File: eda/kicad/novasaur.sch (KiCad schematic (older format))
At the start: 29 parts, among them U1 74F86, U10 74F574, U11 74F574, U12 PAL16R4, U2 74F32, U3 74F11, U4 74F139, U5 74F139, U6 74F157, U7 74F175, U8 74F574, U9 74F138, X1 33M

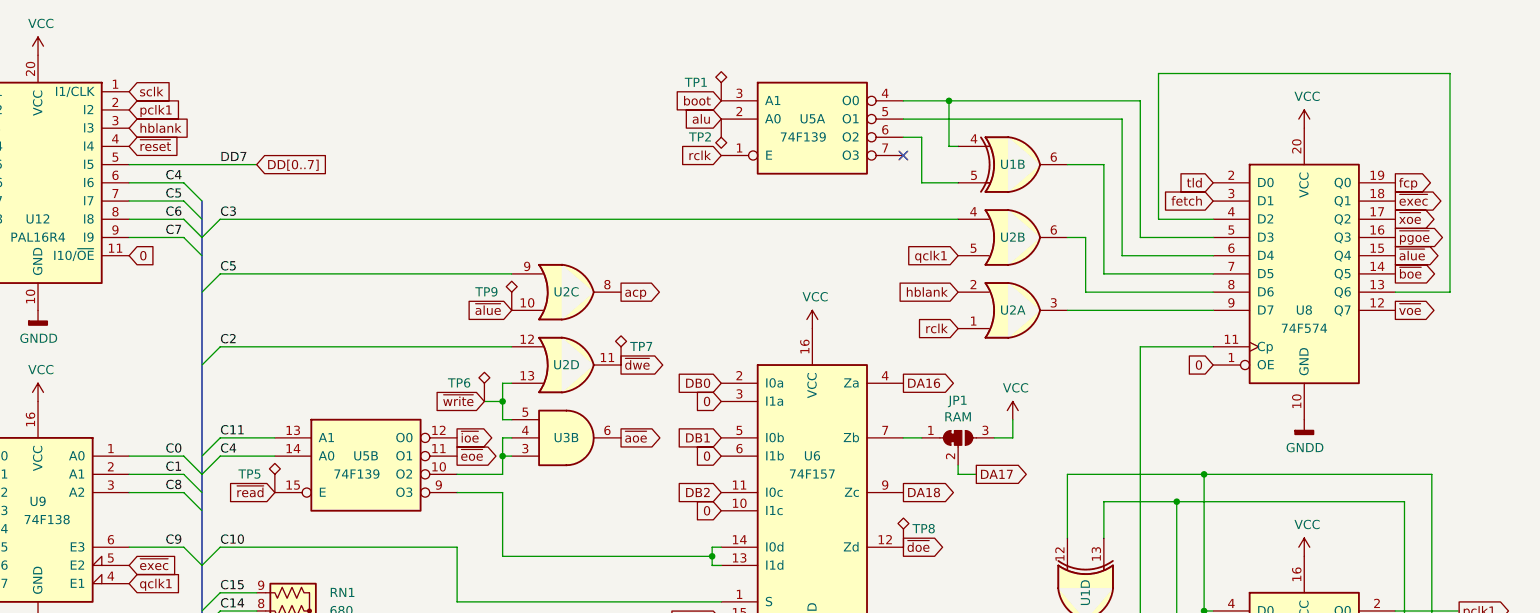
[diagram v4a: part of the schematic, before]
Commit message: roll back to new 6v reg
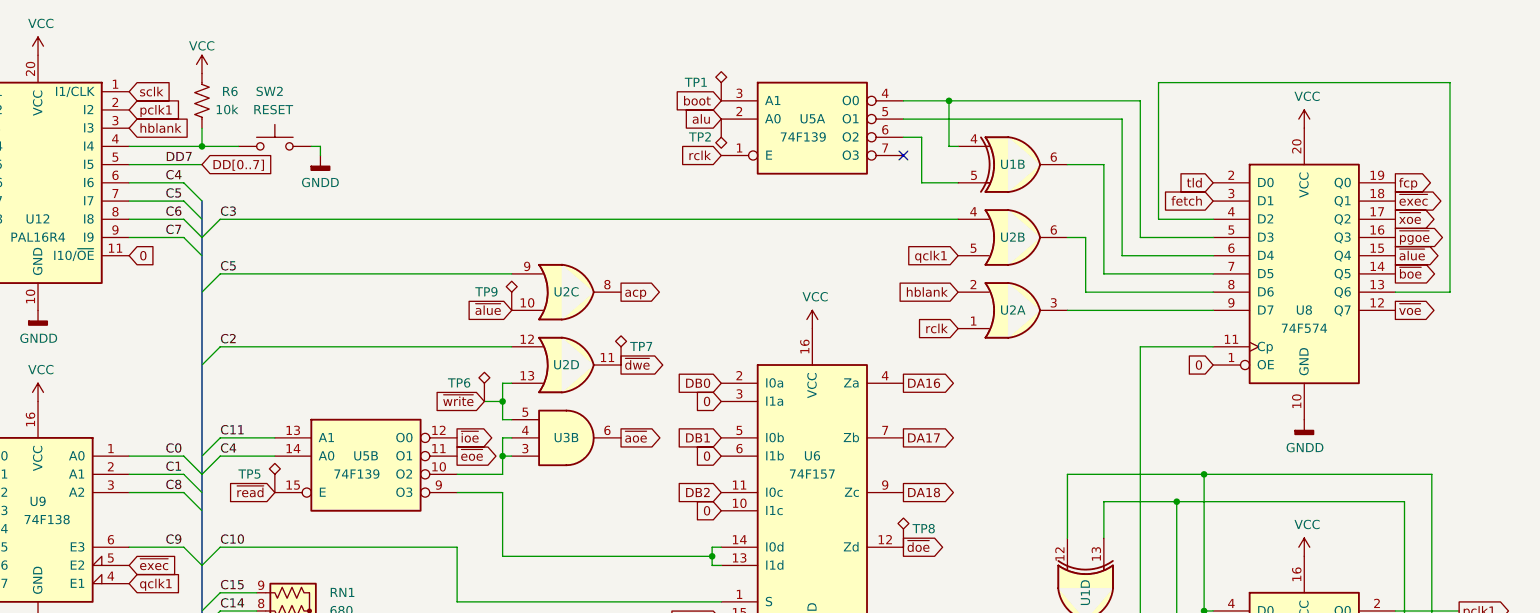
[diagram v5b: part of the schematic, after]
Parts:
- removed JP1: RAM, Jumper:SolderJumper-3_P1.3mm_Bridged12_RoundedPad1.0x1.5mm, symbol Jumper:SolderJumper_3_Bridged12
- added R6: 10k, Resistor_THT:R_Axial_DIN0204_L3.6mm_D1.6mm_P7.62mm_Horizontal, symbol Device:R_US
- added SW2: RESET, Button_Switch_THT:SW_DIP_SPSTx01_Slide_6.7x4.1mm_W7.62mm_P2.54mm_LowProfile, symbol Switch:SW_Push
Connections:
- net DA17: now also U6.7 (Zb)
- net GNDD: now also SW2.1
- net VCC: now also R6.2
- net ~reset: no longer names the net of U12.4 (I4)
- net ~reset: now also R6.1, SW2.2
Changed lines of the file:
@@
 Sheet 1 4
 Title "Novasaur Retrocomputer"
-Date "2021-06-24"
+Date "2021-10-20"
 Rev "1.10"
 Comp ""
@@
 	1    0    0    -1
 $EndComp
-Wire Wire Line
-	9600 1100 8000 1100
 $Comp
 L Connector:TestPoint_Alt TP3
@@
 	7600 4650 7500 4650
 Connection ~ 7600 4650
-Text GLabel 7000 3300 2    50   Output ~ 0
+Text GLabel 6600 3100 2    50   Output ~ 0
 DA17
 Wire Wire Line
 	9600 2300 9300 2300
-Wire Wire Line
-	9600 1100 9600 2300
-Wire Wire Line
-	8000 1100 8000 1900
 Wire Wire Line
 	4400 3000 4400 2900
@@
 	5600 5900 4150 5900
 Connection ~ 4150 5900
-Text GLabel 2350 1500 2    50   Input ~ 0
-~reset
 $Comp
 L Connector:TestPoint_Alt TP28
@@
 F 3 "~" H 4350 5900 50  0001 C CNN
 	1    4150 5900
-	1    0    0    -1
-$EndComp
-Wire Wire Line
-	6600 3100 6700 3100
-$Comp
-L Jumper:SolderJumper_3_Bridged12 JP1
-U 1 1 5EB86903
-P 6900 3100
-F 0 "JP1" H 6900 3305 50  0000 C CNN
-F 1 "RAM" H 6900 3214 50  0000 C CNN
-F 2 "Jumper:SolderJumper-3_P1.3mm_Bridged12_RoundedPad1.0x1.5mm" H 6900 3100 50  0001 C CNN
-F 3 "~" H 6900 3100 50  0001 C CNN
-	1    6900 3100
-	1    0    0    -1
-$EndComp
-Wire Wire Line
-	7000 3300 6900 3300
-Wire Wire Line
-	6900 3300 6900 3250
-Wire Wire Line
-	7100 3100 7200 3100
-Wire Wire Line
-	7200 3100 7200 3000
-$Comp
-L power:VCC #PWR?
-U 1 1 5EAF98E7
-P 7200 3000
-AR Path="/5CDEEC9F/5EAF98E7" Ref="#PWR?"  Part="1"
-AR Path="/5DAA5CD8/5EAF98E7" Ref="#PWR?"  Part="1"
-AR Path="/5EAF98E7" Ref="#PWR0198"  Part="1"
-F 0 "#PWR0198" H 7200 2850 50  0001 C CNN
-F 1 "VCC" H 7217 3173 50  0000 C CNN
-F 2 "" H 7200 3000 50  0001 C CNN
-F 3 "" H 7200 3000 50  0001 C CNN
-	1    7200 3000
 	1    0    0    -1
 $EndComp
@@
 Wire Wire Line
 	9500 4650 9650 4650
-Wire Wire Line
-	2350 1600 3050 1600
-Text Label 2850 1600 0    50   ~ 0
+Text Label 2550 1600 0    50   ~ 0
 DD7
-Text GLabel 3050 1600 2    50   Input ~ 0
+Text GLabel 2750 1600 2    50   Input ~ 0
 DD[0..7]
 $Comp
@@
 Wire Wire Line
 	4150 4000 5600 4000
+$Comp
+L Device:R_US R?
+U 1 1 61FD430E
+P 2750 1250
+AR Path="/62D13D9D/61FD430E" Ref="R?"  Part="1"
+AR Path="/5DAA5CD8/5D9AFF37/61FD430E" Ref="R?"  Part="1"
+AR Path="/5DA1E9C0/61FD430E" Ref="R?"  Part="1"
+AR Path="/61FD430E" Ref="R6"  Part="1"
+F 0 "R6" H 2550 1200 50  0000 L CNN
+F 1 "10k" H 2550 1300 50  0000 L CNN
+F 2 "Resistor_THT:R_Axial_DIN0204_L3.6mm_D1.6mm_P7.62mm_Horizontal" V 2790 1240 50  0001 C CNN
+F 3 "~" H 2750 1250 50  0001 C CNN
+	1    2750 1250
+	-1   0    0    1
+$EndComp
+$Comp
+L Switch:SW_Push SW?
+U 1 1 61FD4314
+P 3150 1500
+AR Path="/5DA1E9C0/61FD4314" Ref="SW?"  Part="1"
+AR Path="/61FD4314" Ref="SW2"  Part="1"
+F 0 "SW2" H 3100 1800 50  0000 L CNN
+F 1 "RESET" H 3050 1700 50  0000 L CNN
+F 2 "Button_Switch_THT:SW_DIP_SPSTx01_Slide_6.7x4.1mm_W7.62mm_P2.54mm_LowProfile" H 3150 1700 50  0001 C CNN
+F 3 "~" H 3150 1700 50  0001 C CNN
+	1    3150 1500
+	-1   0    0    -1
+$EndComp
+Wire Wire Line
+	2750 1500 2750 1400
+Wire Wire Line
+	2350 1500 2750 1500
+$Comp
+L power:GNDD #PWR?
+U 1 1 62E1CD75
+P 3400 1550
+AR Path="/5CDEEC9F/62E1CD75" Ref="#PWR?"  Part="1"
+AR Path="/5DAA5CD8/62E1CD75" Ref="#PWR?"  Part="1"
+AR Path="/62E1CD75" Ref="#PWR0188"  Part="1"
+F 0 "#PWR0188" H 3400 1300 50  0001 C CNN
+F 1 "GNDD" H 3400 1400 50  0000 C CNN
+F 2 "" H 3400 1550 50  0001 C CNN
+F 3 "" H 3400 1550 50  0001 C CNN
+	1    3400 1550
+	1    0    0    -1
+$EndComp
+Wire Wire Line
+	3350 1500 3400 1500
+Wire Wire Line
+	3400 1500 3400 1550
+Connection ~ 2750 1500
+Wire Wire Line
+	2750 1500 2950 1500
+Wire Wire Line
+	8000 1150 9600 1150
+Wire Wire Line
+	8000 1150 8000 1900
+Wire Wire Line
+	9600 1150 9600 2300
+$Comp
+L power:VCC #PWR?
+U 1 1 61743D1E
+P 2750 1100
+AR Path="/5CDEEC9F/61743D1E" Ref="#PWR?"  Part="1"
+AR Path="/5DAA5CD8/61743D1E" Ref="#PWR?"  Part="1"
+AR Path="/61743D1E" Ref="#PWR0111"  Part="1"
+F 0 "#PWR0111" H 2750 950 50  0001 C CNN
+F 1 "VCC" H 2750 1250 50  0000 C CNN
+F 2 "" H 2750 1100 50  0001 C CNN
+F 3 "" H 2750 1100 50  0001 C CNN
+	1    2750 1100
+	1    0    0    -1
+$EndComp
+Wire Wire Line
+	2750 1600 2350 1600
 Wire Bus Line
 	4450 5100 4450 6750

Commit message: tweak schematic; new doc
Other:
- moved on the sheet: TP36, U1D, X1
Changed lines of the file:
@@
 Comment4 ""
 $EndDescr
-Wire Wire Line
-	4650 6000 4650 6700
-Wire Wire Line
-	4250 6000 4250 6550
 Text GLabel 1350 1800 0    50   Output ~ 0
 alu
-Wire Bus Line
-	1150 6850 4350 6850
 Wire Wire Line
 	2450 5700 2650 5700
@@
 	2350 1700 2650 1700
 NoConn ~ 1350 1400
-Entry Bus Bus
-	4350 6850 4450 6750
-Entry Bus Bus
-	1050 6750 1150 6850
 Text GLabel 2350 3900 2    50   Input ~ 0
 qclk1
@@
 Entry Wire Line
 	2650 1700 2750 1800
-Wire Wire Line
-	4250 6000 4150 6000
 $Comp
 L power:GNDD #PWR?
@@
 $EndComp
 Entry Wire Line
-	4450 5100 4350 5000
-Entry Wire Line
-	4450 5200 4350 5100
-Entry Wire Line
-	4450 5300 4350 5200
-Entry Wire Line
-	4450 5800 4350 5700
+	4450 4900 4350 5000
+Entry Wire Line
+	4450 5000 4350 5100
+Entry Wire Line
+	4450 5100 4350 5200
+Entry Wire Line
+	4450 5600 4350 5700
 Text Label 2550 5000 0    50   ~ 0
 C0
@@
 PD[0..7]
 Entry Wire Line
-	4450 5700 4350 5600
-Entry Wire Line
-	4450 5600 4350 5500
-Entry Wire Line
-	4450 5500 4350 5400
-Entry Wire Line
-	4450 5400 4350 5300
+	4450 5500 4350 5600
+Entry Wire Line
+	4450 5400 4350 5500
+Entry Wire Line
+	4450 5300 4350 5400
+Entry Wire Line
+	4450 5200 4350 5300
 Wire Wire Line
 	4150 5000 4350 5000
@@
 	2750 4750 2850 4650
 Wire Wire Line
-	1150 6700 4650 6700
-Wire Wire Line
-	2450 6550 4250 6550
-Wire Wire Line
 	2850 4250 3050 4250
 Wire Wire Line
@@
 Entry Wire Line
 	2850 3200 2750 3300
-Text Notes 3750 7550 0    150  ~ 0
-I/O
-Text Notes 2500 7550 0    150  ~ 0
-GPU
-Text Notes 1300 7550 0    150  ~ 0
-CPU
-$Sheet
-S 1250 7150 600  600
-U 5DA1E9BA
-F0 "sheet5DA1E720" 50
-F1 "novasaur-cpu.sch" 50
-$EndSheet
-$Sheet
-S 2450 7150 600  600
-U 5DA1E9BD
-F0 "sheet5DA1E721" 50
-F1 "novasaur-gpu.sch" 50
-$EndSheet
 Text Label 2850 3700 0    50   ~ 0
 C10
@@
 	1    0    0    -1
 $EndComp
-$Sheet
-S 3650 7150 600  600
-U 5DA1E9C0
-F0 "sheet5DA1E722" 50
-F1 "novasaur-io.sch" 50
-$EndSheet
 $Comp
 L power:VCC #PWR?
@@
 L Connector:TestPoint_Alt TP36
 U 1 1 5E2B88BD
-P 8000 5500
+P 8050 5500
 AR Path="/5E2B88BD" Ref="TP36"  Part="1"
 AR Path="/5DA1E9BA/5E2B88BD" Ref="TP?"  Part="1"
 AR Path="/5DA1E9BD/5E2B88BD" Ref="TP?"  Part="1"
 AR Path="/5DA1E9C0/5E2B88BD" Ref="TP?"  Part="1"
-F 0 "TP36" H 8050 5650 50  0000 L CNN
-F 1 "DCLK" H 7750 5650 50  0001 L CNN
-F 2 "TestPoint:TestPoint_THTPad_1.0x1.0mm_Drill0.5mm" H 8200 5500 50  0001 C CNN
-F 3 "~" H 8200 5500 50  0001 C CNN
-	1    8000 5500
-	1    0    0    -1
-$EndComp
-Wire Wire Line
-	7150 5500 7200 5500
-Wire Wire Line
-	7150 5150 7500 5150
+F 0 "TP36" H 8100 5650 50  0000 L CNN
+F 1 "DCLK" H 7800 5650 50  0001 L CNN
+F 2 "TestPoint:TestPoint_THTPad_1.0x1.0mm_Drill0.5mm" H 8250 5500 50  0001 C CNN
+F 3 "~" H 8250 5500 50  0001 C CNN
+	1    8050 5500
+	1    0    0    -1
+$EndComp
+Wire Wire Line
+	7200 5500 7250 5500
+Wire Wire Line
+	7200 5150 7550 5150
 Wire Wire Line
 	9500 3300 9500 4550
@@
 Wire Wire Line
 	8300 4050 8250 4050
-Text GLabel 7500 4650 0    50   Output ~ 0
+Text GLabel 7600 4650 0    50   Output ~ 0
 nclk
 NoConn ~ 9300 4750
 Wire Wire Line
-	7500 5150 7500 5100
-Connection ~ 7500 5150
-Wire Wire Line
-	7500 5200 7500 5150
+	7550 5150 7550 5100
+Connection ~ 7550 5150
+Wire Wire Line
+	7550 5200 7550 5150
 Wire Wire Line
 	9350 4250 9650 4250
@@
 L Oscillator:CXO_DIP8 X1
 U 1 1 5D9CA9D5
-P 7500 5500
-F 0 "X1" H 7650 5900 50  0000 L CNN
-F 1 "33M" H 7600 5800 50  0000 L CNN
-F 2 "Oscillator:Oscillator_DIP-8" H 7950 5150 50  0001 C CNN
-F 3 "http://cdn-reichelt.de/documents/datenblatt/B400/OSZI.pdf" H 7400 5500 50  0001 C CNN
-	1    7500 5500
+P 7550 5500
+F 0 "X1" H 7700 5900 50  0000 L CNN
+F 1 "33M" H 7650 5800 50  0000 L CNN
+F 2 "Oscillator:Oscillator_DIP-8" H 8000 5150 50  0001 C CNN
+F 3 "http://cdn-reichelt.de/documents/datenblatt/B400/OSZI.pdf" H 7450 5500 50  0001 C CNN
+	1    7550 5500
 	1    0    0    -1
 $EndComp
@@
 L power:GNDD #PWR?
 U 1 1 5D9CBE89
-P 7500 5800
+P 7550 5800
 AR Path="/5CDEEC9F/5D9CBE89" Ref="#PWR?"  Part="1"
 AR Path="/5DAA5CD8/5D9CBE89" Ref="#PWR?"  Part="1"
 AR Path="/5D9CBE89" Ref="#PWR0112"  Part="1"
-F 0 "#PWR0112" H 7500 5550 50  0001 C CNN
-F 1 "GNDD" H 7504 5645 50  0000 C CNN
-F 2 "" H 7500 5800 50  0001 C CNN
-F 3 "" H 7500 5800 50  0001 C CNN
-	1    7500 5800
+F 0 "#PWR0112" H 7550 5550 50  0001 C CNN
+F 1 "GNDD" H 7554 5645 50  0000 C CNN
+F 2 "" H 7550 5800 50  0001 C CNN
+F 3 "" H 7550 5800 50  0001 C CNN
+	1    7550 5800
 	1    0    0    -1
 $EndComp
@@
 L power:VCC #PWR0191
 U 1 1 5D9DED2A
-P 7500 5100
+P 7550 5100
 AR Path="/5D9DED2A" Ref="#PWR0191"  Part="1"
 AR Path="/5DAA5CD8/5D9DED2A" Ref="#PWR?"  Part="1"
-F 0 "#PWR0191" H 7500 4950 50  0001 C CNN
-F 1 "VCC" H 7517 5273 50  0000 C CNN
-F 2 "" H 7500 5100 50  0001 C CNN
-F 3 "" H 7500 5100 50  0001 C CNN
-	1    7500 5100
-	1    0    0    -1
-$EndComp
-Text GLabel 8000 5500 2    50   Output ~ 0
+F 0 "#PWR0191" H 7550 4950 50  0001 C CNN
+F 1 "VCC" H 7567 5273 50  0000 C CNN
+F 2 "" H 7550 5100 50  0001 C CNN
+F 3 "" H 7550 5100 50  0001 C CNN
+	1    7550 5100
+	1    0    0    -1
+$EndComp
+Text GLabel 8050 5500 2    50   Output ~ 0
 dclk
 $Comp
@@
 DB2
 Wire Wire Line
-	7600 4650 7600 4250
+	7700 4650 7700 4250
 $Comp
 L Connector:TestPoint_Alt TP10
@@
 $EndComp
 Wire Wire Line
-	7600 4650 7500 4650
-Connection ~ 7600 4650
+	7700 4650 7600 4650
+Connection ~ 7700 4650
 Text GLabel 6600 3100 2    50   Output ~ 0
 DA17
@@
 	8250 4050 8250 3300
 Wire Wire Line
-	8250 3300 9500 3300
-Wire Wire Line
 	8100 4450 8100 3450
 Connection ~ 8100 3450
 Wire Wire Line
 	8100 4450 8300 4450
-Wire Wire Line
-	8100 3450 9350 3450
 Connection ~ 8250 3300
 Wire Wire Line
-	7900 4850 8300 4850
-Wire Wire Line
-	7500 3650 7500 3300
-Wire Wire Line
-	7500 3300 8250 3300
-Wire Wire Line
-	7700 3650 7700 3450
-Wire Wire Line
-	7700 3450 8100 3450
-Wire Wire Line
-	7900 2600 8300 2600
+	7600 3650 7600 3300
+Wire Wire Line
+	7600 3300 8250 3300
+Wire Wire Line
+	7800 3650 7800 3450
+Wire Wire Line
+	7800 3450 8100 3450
 Wire Wire Line
 	4400 3750 5550 3750
 Wire Wire Line
 	2850 1900 6900 1900
-Wire Wire Line
-	4650 6000 5600 6000
-Wire Wire Line
-	7800 5500 7900 5500
-Connection ~ 7900 5500
-Wire Wire Line
-	7900 5500 8000 5500
 Wire Wire Line
 	4450 3200 4400 3200
@@
 	4400 2900 4400 2800
 Wire Wire Line
-	7150 5150 7150 5500
-Wire Wire Line
-	7900 4850 7900 5500
-Wire Wire Line
-	7600 4650 8300 4650
-Wire Wire Line
-	7900 4850 7900 2600
-Connection ~ 7900 4850
+	7200 5150 7200 5500
+Wire Wire Line
+	7700 4650 8300 4650
 Wire Wire Line
 	4400 3750 4400 3400
@@
 	1    0    0    -1
 $EndComp
-Wire Wire Line
-	1150 6700 1150 5900
-Wire Wire Line
-	1150 5900 1350 5900
 Connection ~ 1350 5900
 Wire Wire Line
@@
 L 74xx:74LS86 U1
 U 4 1 5F86670E
-P 7600 3950
+P 7700 3950
 AR Path="/5F86670E" Ref="U1"  Part="4"
 AR Path="/5DA1E9BD/5F86670E" Ref="U?"  Part="4"
 AR Path="/5DA1E9BA/5F86670E" Ref="U?"  Part="4"
-F 0 "U1" H 7600 3950 50  0000 C CNN
-F 1 "74F86" H 7600 4184 50  0001 C CNN
-F 2 "Package_DIP:DIP-14_W7.62mm_LongPads" H 7600 3950 50  0001 C CNN
-F 3 "74xx/74ls86.pdf" H 7600 3950 50  0001 C CNN
-	4    7600 3950
+F 0 "U1" H 7700 3950 50  0000 C CNN
+F 1 "74F86" H 7700 4184 50  0001 C CNN
+F 2 "Package_DIP:DIP-14_W7.62mm_LongPads" H 7700 3950 50  0001 C CNN
+F 3 "74xx/74ls86.pdf" H 7700 3950 50  0001 C CNN
+	4    7700 3950
 	0    -1   1    0
 $EndComp
@@
 Wire Wire Line
 	2750 1600 2350 1600
+Wire Wire Line
+	1200 5900 1200 6700
+Wire Wire Line
+	1200 5900 1350 5900
+Wire Wire Line
+	1200 6700 4600 6700
+Wire Wire Line
+	4600 6700 4600 6000
+Wire Wire Line
+	4600 6000 5600 6000
+Wire Wire Line
+	4300 6550 4300 6000
+Wire Wire Line
+	4150 6000 4300 6000
+Wire Wire Line
+	2450 6550 4300 6550
+Wire Wire Line
+	8100 3450 9350 3450
+Wire Wire Line
+	8250 3300 9500 3300
+Wire Wire Line
+	7950 5500 7950 4850
+Wire Wire Line
+	7950 2600 8300 2600
+Wire Wire Line
+	7950 4850 8300 4850
+Connection ~ 7950 4850
+Wire Wire Line
+	7950 4850 7950 2600
+Wire Wire Line
+	7850 5500 7950 5500
+Wire Wire Line
+	7950 5500 8050 5500
+Connection ~ 7950 5500
+Text GLabel 4450 4700 1    50   Input ~ 0
+PD[0..7]
+Text Notes 3750 7500 0    150  ~ 0
+I/O
+Text Notes 2500 7500 0    150  ~ 0
+GPU
+Text Notes 1300 7500 0    150  ~ 0
+CPU
+$Sheet
+S 1250 7100 600  600
+U 5DA1E9BA
+F0 "sheet5DA1E720" 50
+F1 "novasaur-cpu.sch" 50
+$EndSheet
+$Sheet
+S 2450 7100 600  600
+U 5DA1E9BD
+F0 "sheet5DA1E721" 50
+F1 "novasaur-gpu.sch" 50
+$EndSheet
+$Sheet
+S 3650 7100 600  600
+U 5DA1E9C0
+F0 "sheet5DA1E722" 50
+F1 "novasaur-io.sch" 50
+$EndSheet
 Wire Bus Line
-	4450 5100 4450 6750
+	4450 4700 4450 5600
 Wire Bus Line
-	1050 4700 1050 6750
+	1050 4700 1050 5600
 Wire Bus Line
 	2750 1800 2750 6000

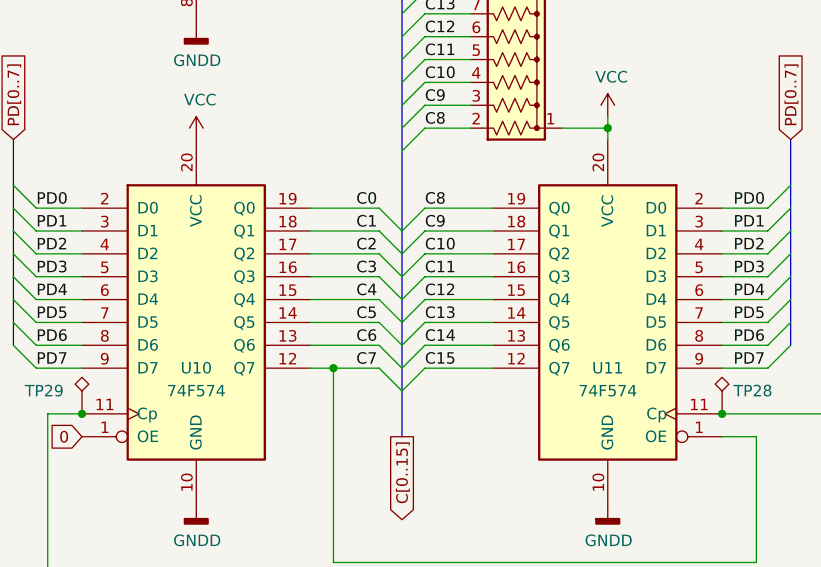
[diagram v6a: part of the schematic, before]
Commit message: annotate registers
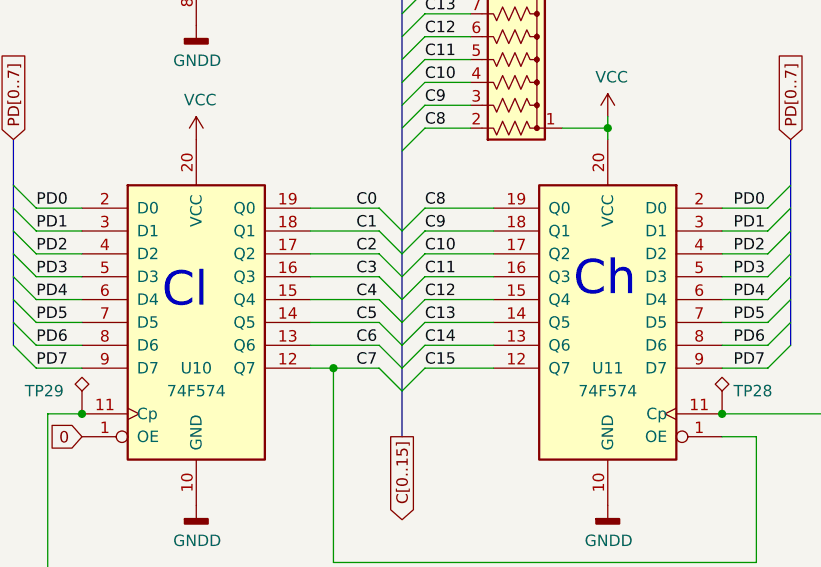
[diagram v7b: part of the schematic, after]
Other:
- note added: "Ch"
- note added: "Cl"
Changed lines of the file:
@@
 Sheet 1 4
 Title "Novasaur Retrocomputer"
-Date "2021-10-20"
+Date "2021-11-20"
 Rev "1.10"
 Comp ""
@@
 F1 "novasaur-io.sch" 50
 $EndSheet
+Text Notes 1700 5450 0    150  ~ 0
+Cl
+Text Notes 3500 5400 0    150  ~ 0
+Ch
 Wire Bus Line
 	4450 4700 4450 5600
